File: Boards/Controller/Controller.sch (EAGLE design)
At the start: 9 parts

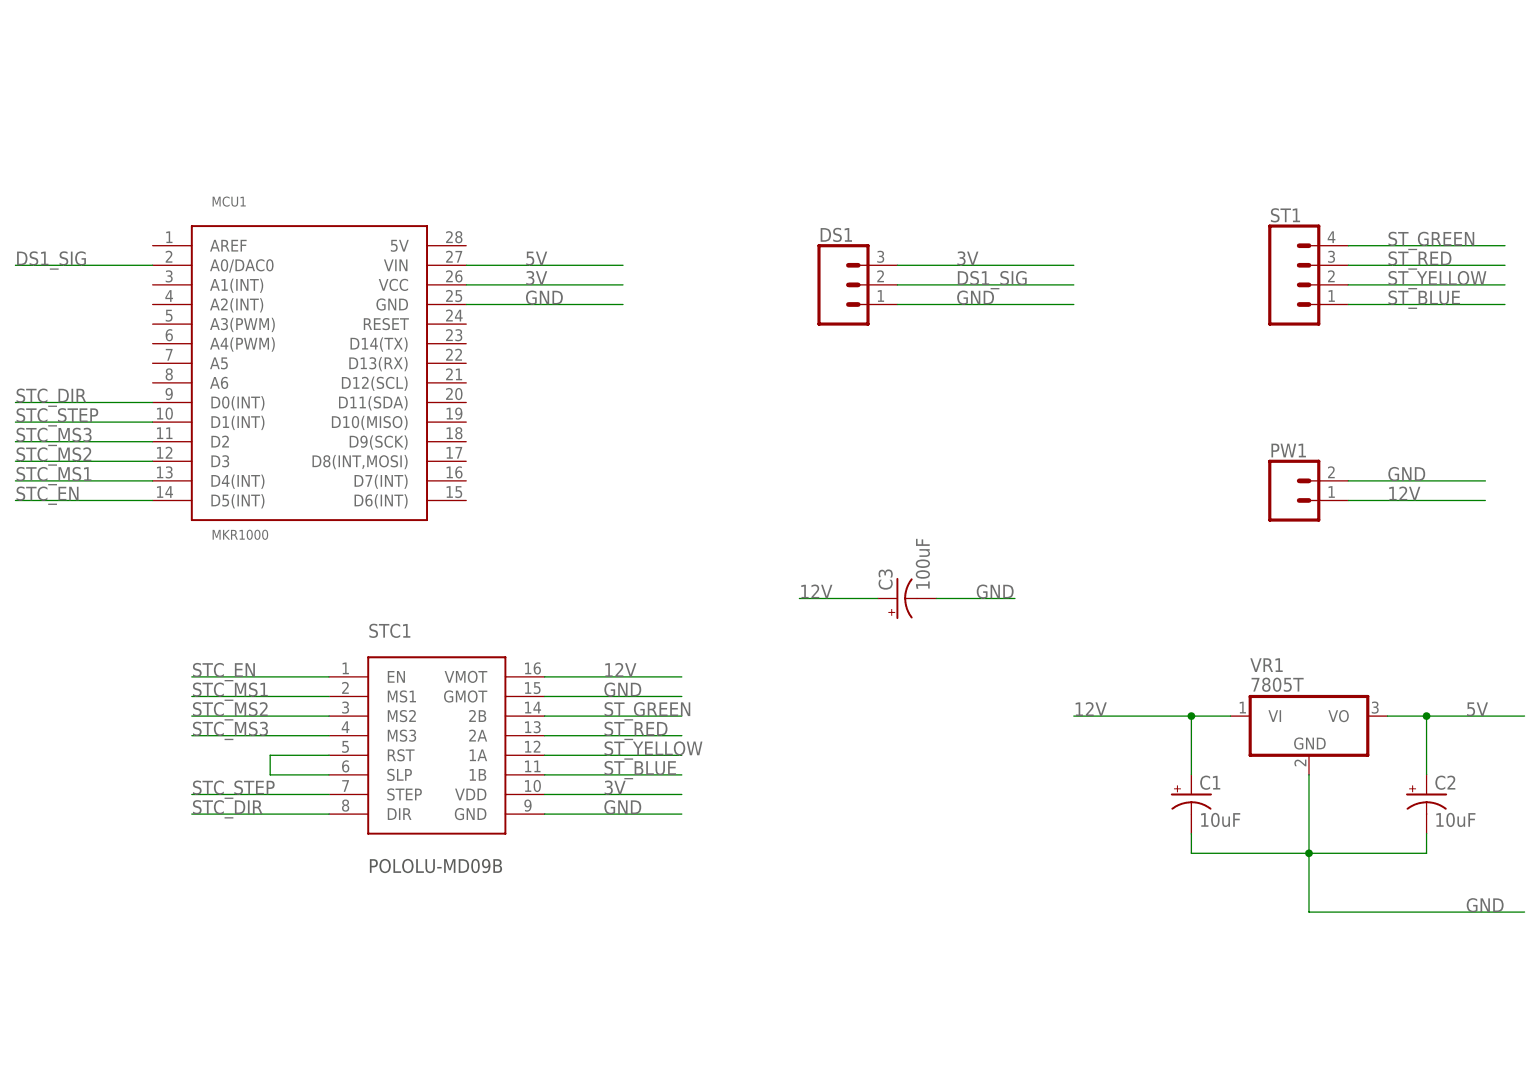
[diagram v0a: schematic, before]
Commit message: finished controller for mass production
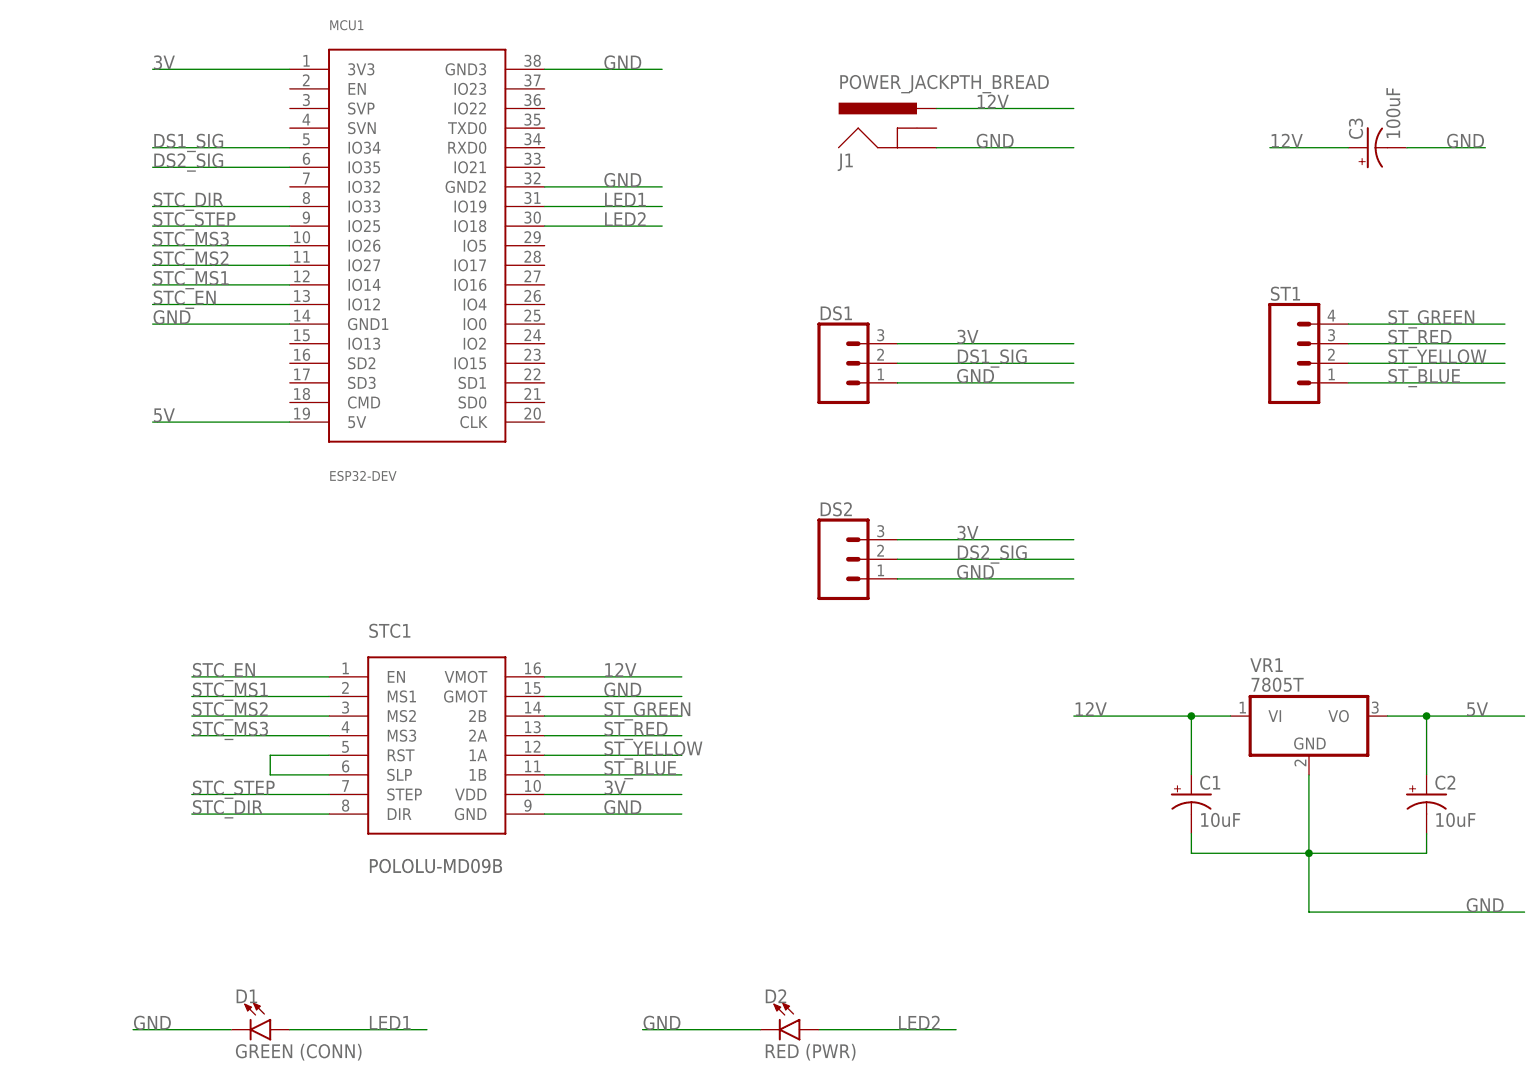
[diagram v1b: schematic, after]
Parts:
- removed PW1: (no value), SparkFun-Connectors:CONN_025MM
- added D1: GREEN (CONN), SparkFun-LED:LED5MM
- added D2: RED (PWR), SparkFun-LED:LED5MM
- added DS2: (no value), SparkFun-Connectors:CONN_03LONGPADS
- added J1: POWER_JACKPTH_BREAD, SparkFun-Connectors:POWER_JACKPTH_BREAD
- MCU1: value MKR1000 -> ESP32-DEV; device Library:MKR1000 -> IAD-Library:ESP32-DEV
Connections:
- new net DS2_SIG: DS2.2, MCU1.IO35
- new net LED1: D1.A, MCU1.IO19
- new net LED2: D2.A, MCU1.IO18
- net 12V: now also J1.PWR; no longer PW1.1
- net 3V: now also DS2.3, MCU1.3V3; no longer MCU1.VCC
- net 5V: now also MCU1.5V; no longer MCU1.VIN
- net DS1_SIG: now also MCU1.IO34; no longer MCU1.A0/DAC0
- net GND: now also D1.C, D2.C, DS2.1, J1.GND, MCU1.GND1, MCU1.GND2, MCU1.GND3; no longer MCU1.GND, PW1.2
- net STC_DIR: now also MCU1.IO33; no longer MCU1.D0(INT)
- net STC_EN: now also MCU1.IO12; no longer MCU1.D5(INT)
- net STC_MS1: now also MCU1.IO14; no longer MCU1.D4(INT)
- net STC_MS2: now also MCU1.IO27; no longer MCU1.D3
- net STC_MS3: now also MCU1.IO26; no longer MCU1.D2
- net STC_STEP: now also MCU1.IO25; no longer MCU1.D1(INT)
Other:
- moved on the sheet: C3, DS1, ST1

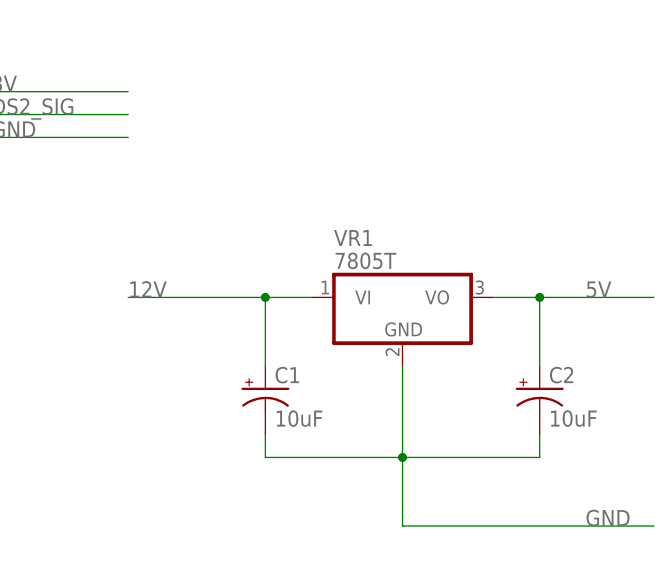
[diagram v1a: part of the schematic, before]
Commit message: use stepping voltage regulator instead of a linear
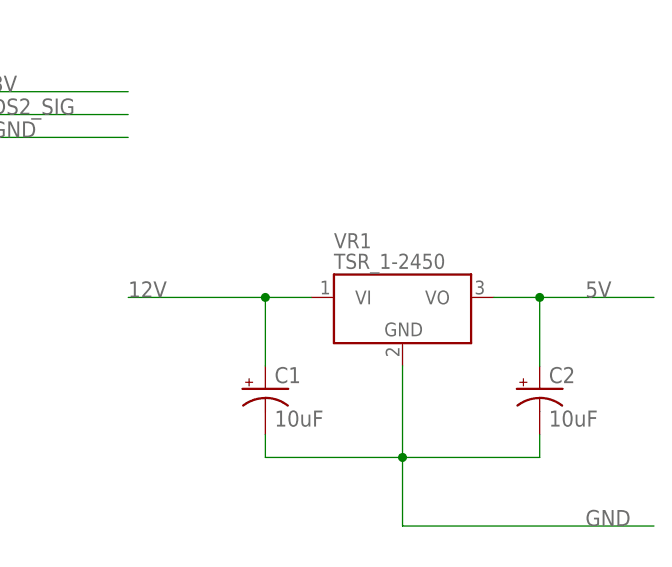
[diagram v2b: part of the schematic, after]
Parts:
- VR1: value 7805T -> TSR_1-2450; device adafruit:7805T -> Traco-TSR1:TSR_1-2450
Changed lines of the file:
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@@
 <part name="STC1" library="Library" deviceset="POLOLU-MD09B" device=""/>
 <part name="ST1" library="SparkFun-Connectors" deviceset="CONN_04" device="LONGPADS"/>
-<part name="VR1" library="adafruit" deviceset="78*" device="T" technology="05"/>
+<part name="VR1" library="Traco-TSR1" deviceset="TSR_1-*" device="" technology="2450"/>
 <part name="C1" library="adafruit" deviceset="CPOL-US" device="E2-5" value="10uF"/>
 <part name="C2" library="adafruit" deviceset="CPOL-US" device="E2-5" value="10uF"/>
@@
 <instance part="STC1" gate="G$1" x="48.26" y="12.7"/>
 <instance part="ST1" gate="G$1" x="160.02" y="63.5"/>
-<instance part="VR1" gate="A1" x="160.02" y="17.78"/>
+<instance part="VR1" gate="G$1" x="160.02" y="17.78"/>
 <instance part="C1" gate="G$1" x="144.78" y="7.62"/>
 <instance part="C2" gate="G$1" x="175.26" y="7.62"/>
@@
 </segment>
 <segment>
-<pinref part="VR1" gate="A1" pin="GND"/>
+<pinref part="VR1" gate="G$1" pin="GND"/>
 <wire x1="160.02" y1="10.16" x2="160.02" y2="0" width="0.1524" layer="91"/>
 <pinref part="C1" gate="G$1" pin="-"/>
@@
 </segment>
 <segment>
-<pinref part="VR1" gate="A1" pin="VI"/>
+<pinref part="VR1" gate="G$1" pin="VI"/>
 <wire x1="149.86" y1="17.78" x2="144.78" y2="17.78" width="0.1524" layer="91"/>
 <pinref part="C1" gate="G$1" pin="+"/>
@@
 <net name="5V" class="0">
 <segment>
-<pinref part="VR1" gate="A1" pin="VO"/>
+<pinref part="VR1" gate="G$1" pin="VO"/>
 <wire x1="170.18" y1="17.78" x2="175.26" y2="17.78" width="0.1524" layer="91"/>
 <pinref part="C2" gate="G$1" pin="+"/>
